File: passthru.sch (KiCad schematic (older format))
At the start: 0 parts

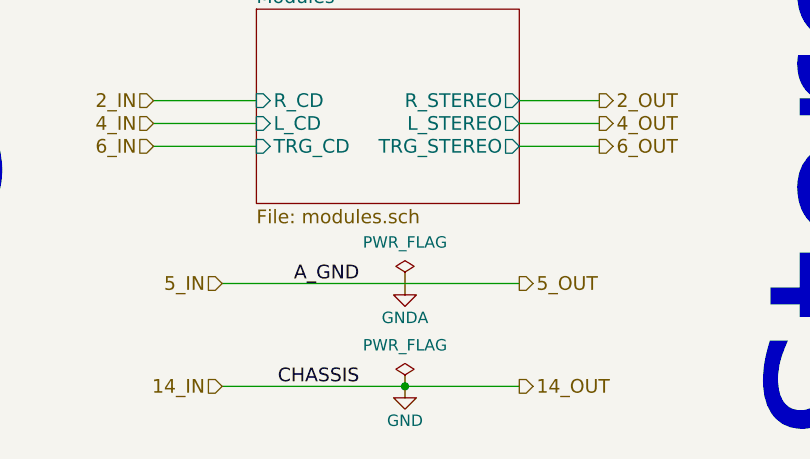
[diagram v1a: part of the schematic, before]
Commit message: Fix lack of junction to GNDA, and route traces.
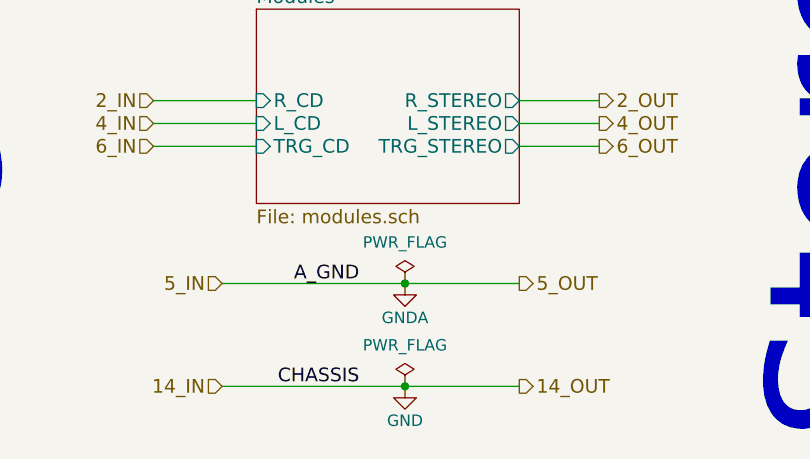
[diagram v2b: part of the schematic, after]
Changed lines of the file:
@@
 Text Label 5500 1750 2    60   ~ 0
 R
+Connection ~ 5650 5150
 $EndSCHEMATC
